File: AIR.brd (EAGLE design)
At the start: 100 x 47 mm, 32 parts

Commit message: Updated EAGLE files
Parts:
- CE1, CE2, CE3, CE4: value 100uF -> 100µF
- moved C10 12.7 mm to (81.0, 41.5)
- moved MAINS/BATT 8.26 mm to (78.0, 9.38)
- moved C6 0.52 mm to (82.0, 30.2)
- moved C5 0.40 mm to (42.3, 41.6)
- moved C7 0.25 mm to (82.0, 22.5)
- moved C1 0.25 mm to (31.2, 30.1)
- moved C4 0.25 mm to (41.3, 30.1)
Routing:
- net N$3: track 9.72 -> 18.0 mm
- net GND: track 352.6 -> 355.0 mm
- net D9~: track 14.1 -> 14.7 mm
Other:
- outline, holes or cut-outs redrawn
- board text added: "MOTOR TERMINALS: B L R C +-"
- board text added: "Micmind Air P3 http://micmind.pooledge.net"
- board text removed: "B L R C + -"
- board text removed: "Micmind Air P3 http://www.pooledge.net/micmind"

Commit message: Major improvements on hardware, patch stability
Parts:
- removed MAINS/BATT, MOT/B, MOT/C, MOT/L, MOT/R: 691101710002, Wurth_Elektronik_Electromechanic_Terminal_Blocks_Connectors_rev15b:691101710002
- added BATT/CHRG: 691121710004, Wurth_Elektronik_Electromechanic_Terminal_Blocks_Connectors_rev15b:691121710004
- added MOTORS/BLCR: 691221320008, Wurth_Elektronik_Electromechanic_Terminal_Blocks_Connectors_rev15b:691221320008
- MAINS/SW: value 691101710002 -> 691101710003; device Wurth_Elektronik_Electromechanic_Terminal_Blocks_Connectors_rev15b:691101710002 -> Wurth_Elektronik_Electromechanic_Terminal_Blocks_Connectors_rev15b:691101710003
- moved MAINS/SW 7.24 mm to (60.7, 17.0), turned to 0 degrees
- moved ABPROMINI/2 3.70 mm to (62.3, 42.2)
- moved ABPROMINI/1 3.70 mm to (62.3, 26.9)
- moved DCDCCONV 2.01 mm to (47.0, 13.6), turned to 270 degrees
- moved C6 1.35 mm to (80.6, 30.1)
- moved C7 1.27 mm to (80.8, 22.5)
- moved C8 1.27 mm to (91.0, 22.5)
- moved C9 1.27 mm to (90.7, 30.1)
- moved CE3 1.27 mm to (85.8, 11.7)
- moved CE4 1.27 mm to (85.8, 40.9)
- moved L293D2/1 1.27 mm to (83.2, 26.3)
- moved L293D2/2 1.27 mm to (88.3, 26.3)
- moved C5 0.70 mm to (41.6, 41.5)
- moved C10 0.64 mm to (80.4, 41.5)
- moved XB/LEDASC 0.38 mm to (27.2, 44.1)
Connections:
- new net N$4: BATT/CHRG.4, MAINS/SW.3
- net +24V: now also MAINS/SW.1; no longer MAINS/SW.2
- net GND: now also BATT/CHRG.2, BATT/CHRG.3; no longer MAINS/BATT.2
- net MB+: now also MOTORS/BLCR.1; no longer MOT/B.1
- net MB-: now also MOTORS/BLCR.2; no longer MOT/B.2
- net MC+: now also MOTORS/BLCR.5; no longer MOT/C.1
- net MC-: now also MOTORS/BLCR.6; no longer MOT/C.2
- net ML+: now also MOTORS/BLCR.3; no longer MOT/L.1
- net ML-: now also MOTORS/BLCR.4; no longer MOT/L.2
- net MR+: now also MOTORS/BLCR.7; no longer MOT/R.1
- net MR-: now also MOTORS/BLCR.8; no longer MOT/R.2
- net N$3: now also BATT/CHRG.1, MAINS/SW.2; no longer MAINS/BATT.1, MAINS/SW.1
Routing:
- net MC-: track 87.3 -> 142.3 mm, vias 2 -> 0
- net MC+: track 76.4 -> 124.6 mm, vias 1 -> 0
- net D4: track 54.3 -> 32.5 mm
- net MB-: track 121.6 -> 143.3 mm
- net MB+: track 133.1 -> 151.8 mm
- net N$4: track 0.00 -> 10.6 mm
- net +5V: track 162.9 -> 171.3 mm, vias 1 -> 0
- net N$3: track 18.0 -> 10.1 mm
- net D6~: track 23.2 -> 30.6 mm
- net D8: track 24.5 -> 17.5 mm
- net A1: track 44.1 -> 50.4 mm
- net MR+: track 14.7 -> 20.4 mm
- net MR-: track 9.26 -> 14.9 mm
- net ML+: track 32.3 -> 27.6 mm
- net D3: track 48.9 -> 44.6 mm
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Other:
- board size 100 x 47 mm -> 100 x 48 mm
- board text added: "B/L/C/R +-"
- board text added: "BATT+/BATT-/CHRG-/CHRG+"
- board text added: "I / O / II"
- board text added: "LED/G/ASC/G/RSSI"
- board text removed: "LED G ASC G RSSI"
- board text removed: "MAINS SW"
- board text removed: "MOTOR TERMINALS: B L R C +-"

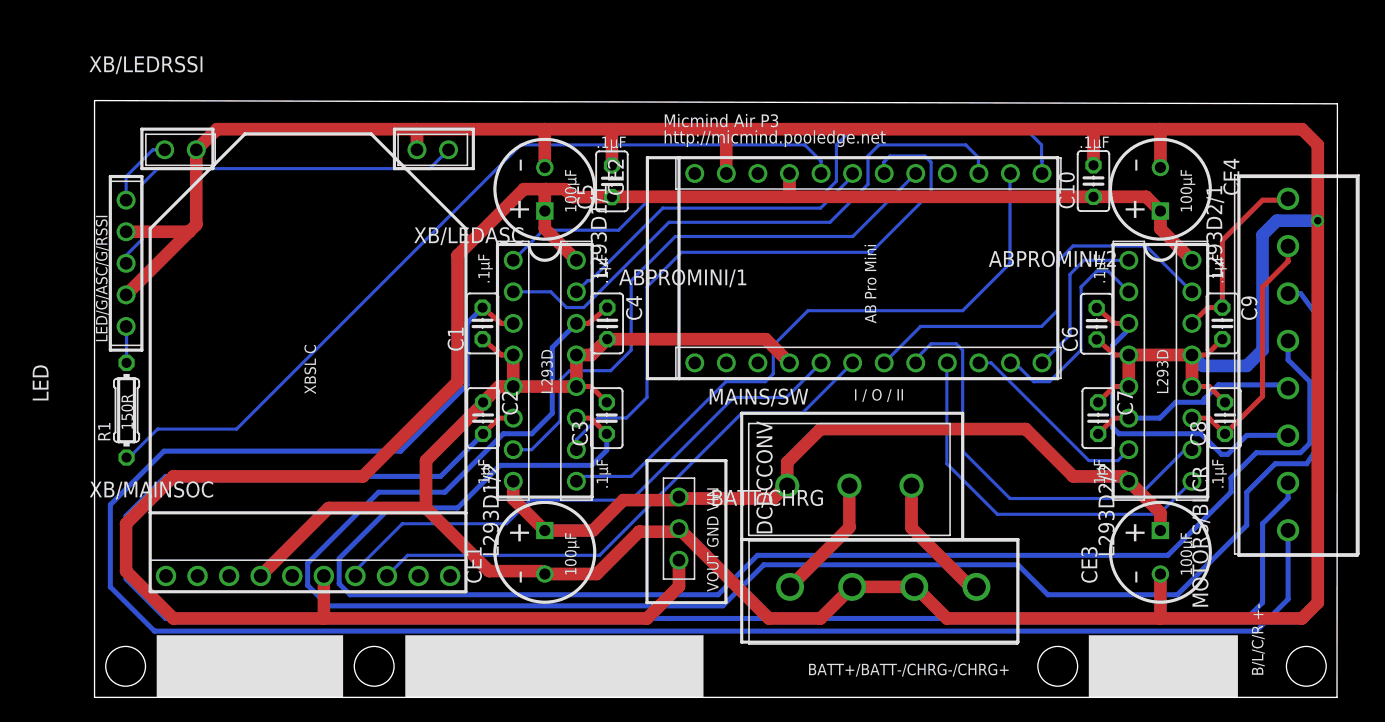
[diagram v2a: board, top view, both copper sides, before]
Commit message: PCB updated for integration with LEGO
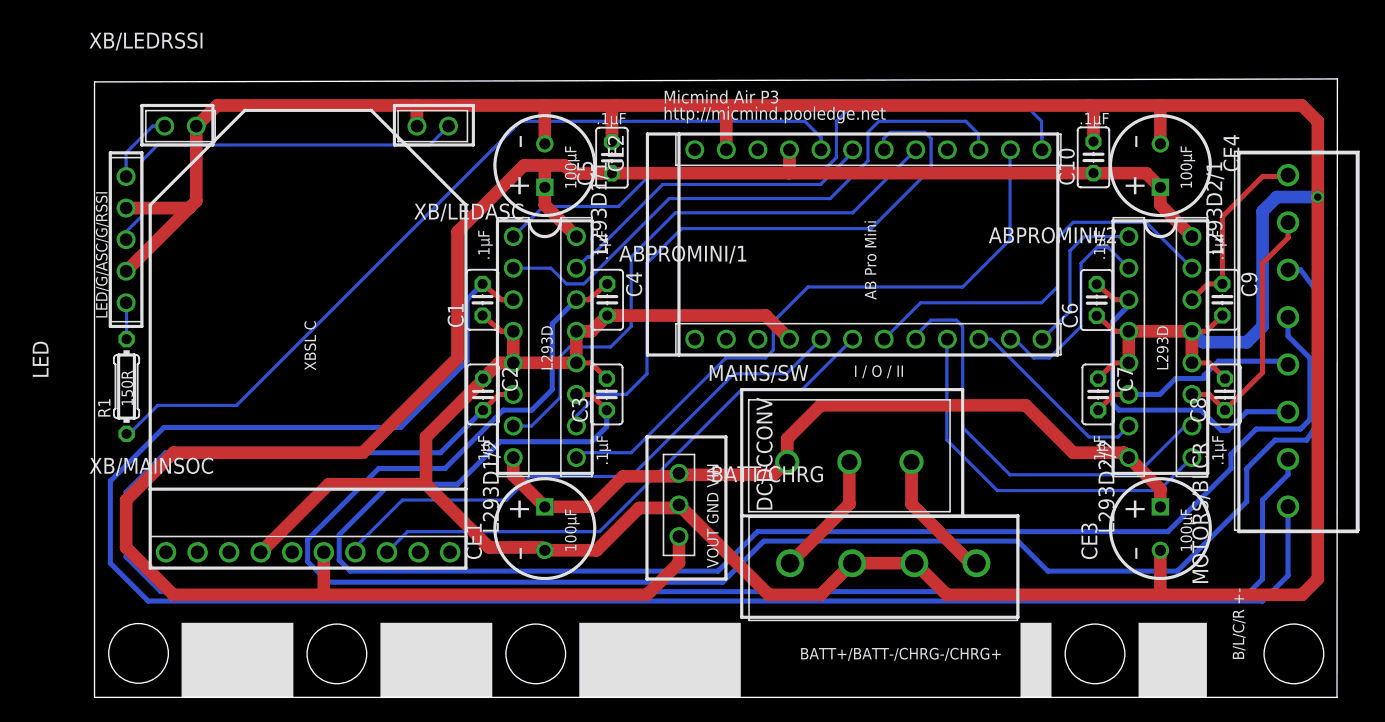
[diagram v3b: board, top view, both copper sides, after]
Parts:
- moved ABPROMINI/1 1.91 mm to (62.3, 28.8)
- moved ABPROMINI/2 1.91 mm to (62.3, 44.1)
- moved C1 1.91 mm to (31.2, 32.0)
- moved C10 1.91 mm to (80.4, 43.5)
- moved C2 1.91 mm to (31.3, 24.4)
- moved C3 1.91 mm to (41.2, 24.4)
- moved C4 1.91 mm to (41.3, 32.0)
- moved C6 1.91 mm to (80.6, 32.0)
- moved C7 1.91 mm to (80.8, 24.4)
- moved C8 1.91 mm to (91.0, 24.4)
- moved C9 1.91 mm to (90.7, 32.0)
- moved CE2 1.91 mm to (36.2, 42.8)
- moved CE4 1.91 mm to (85.8, 42.8)
- moved LED 1.91 mm to (2.54, 36.8)
- moved MAINS/SW 1.91 mm to (60.7, 18.9)
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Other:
- board size 100 x 48 mm -> 100 x 49.8 mm
